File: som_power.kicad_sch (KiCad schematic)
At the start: 123 parts, among them J1 Hermaphroditic_Molex_203456-0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, Q10 DMG1012T-7, Q11 DMG1012T-7, Q17 DMG1012T-7, Q18 DMG1012T-7, Q20 DMG1012T-7, Q22 DMG1012T-7, Q30 DMG1012T-7, Q37 DMG1012T-7, Q38 DMG1012T-7, Q40 DMG1012T-7, Q7 DMG1012T-7, Q8 DMG1012T-7, SW2 SW_SPDT_PCM12SMTR, U3 LTC6994CDCB-1_DFN, U70 MAX16150A_SOT, U72 TPS3840PL30DBVR, U74 SN74LVC2G07DCKR

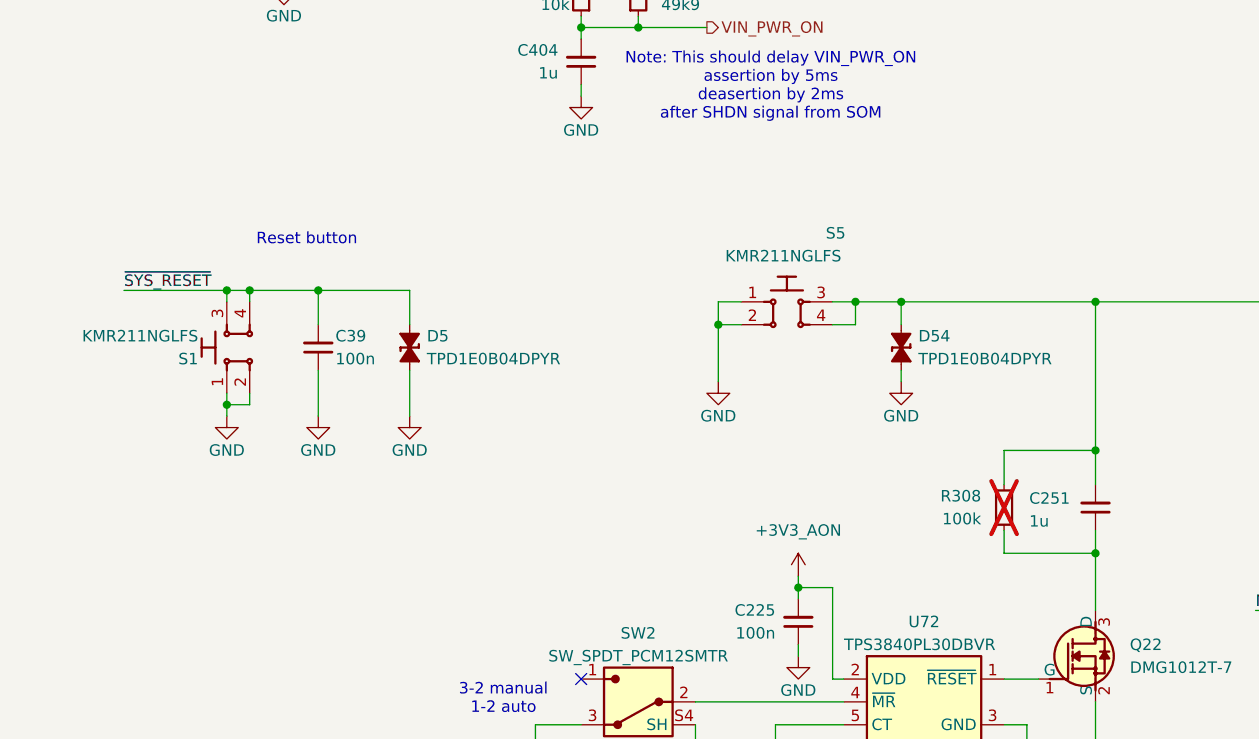
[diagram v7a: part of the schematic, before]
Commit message: [#89536] Add LED driven by SYS_RESET_N signal
Used as boot LED
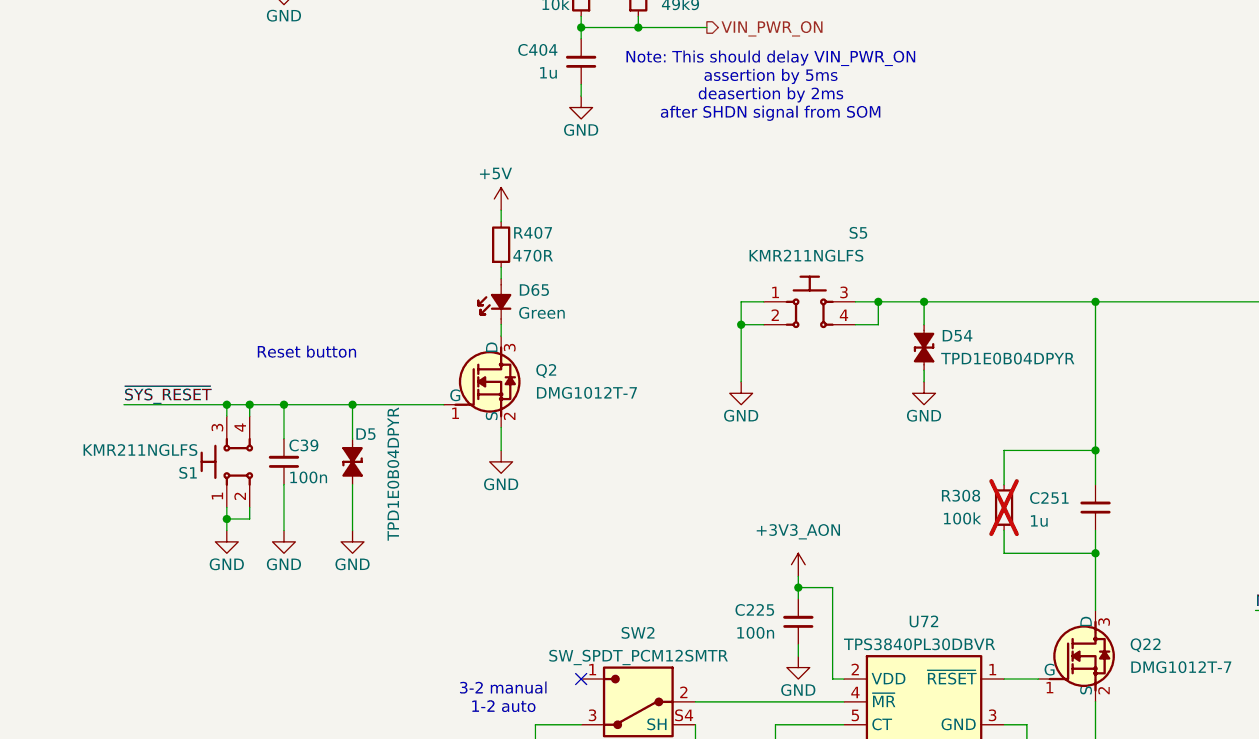
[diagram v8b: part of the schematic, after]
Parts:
- added D65: LED_G_0603_LTST-C190GKT, antmicro-footprints:LED_0603_1608Metric_G, symbol antmicroLEDIndicationDiscrete:LED_G_0603_LTST-C190GKT
- added Q2: DMG1012T-7, antmicro-footprints:SOT-523, symbol antmicroTransistorsFETsMOSFETsSingle:DMG1012T-7
- added R407: R_470R_0402, antmicro-footprints:R_0402_1005Metric, symbol antmicroResistors0402:R_470R_0402
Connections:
- net +5V: now also R407.2
- net GND: now also Q2.2 (S)
- net ~{SYS_RESET}: now also Q2.1 (G)
- new net: D65.1 (C), Q2.3 (D)
- new net: D65.2 (A), R407.1
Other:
- moved on the sheet: C39, D5, D54, S1, S5
